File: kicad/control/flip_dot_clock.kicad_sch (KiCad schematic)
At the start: 36 parts, among them J1 Conn_01x02_Male, J2 Conn_02x08_Odd_Even, J3 Conn_01x05_Male, U1 NUCLEO-F303K8-HEADER, U10 Small_7_Seg_FlipDot_Module, U2 SLC03B-05, U3 NCV7719, U4 Small_7_Seg_FlipDot_Module, U5 NCV7719, U6 Small_7_Seg_FlipDot_Module, U7 NCV7719, U8 Small_7_Seg_FlipDot_Module, U9 NCV7719

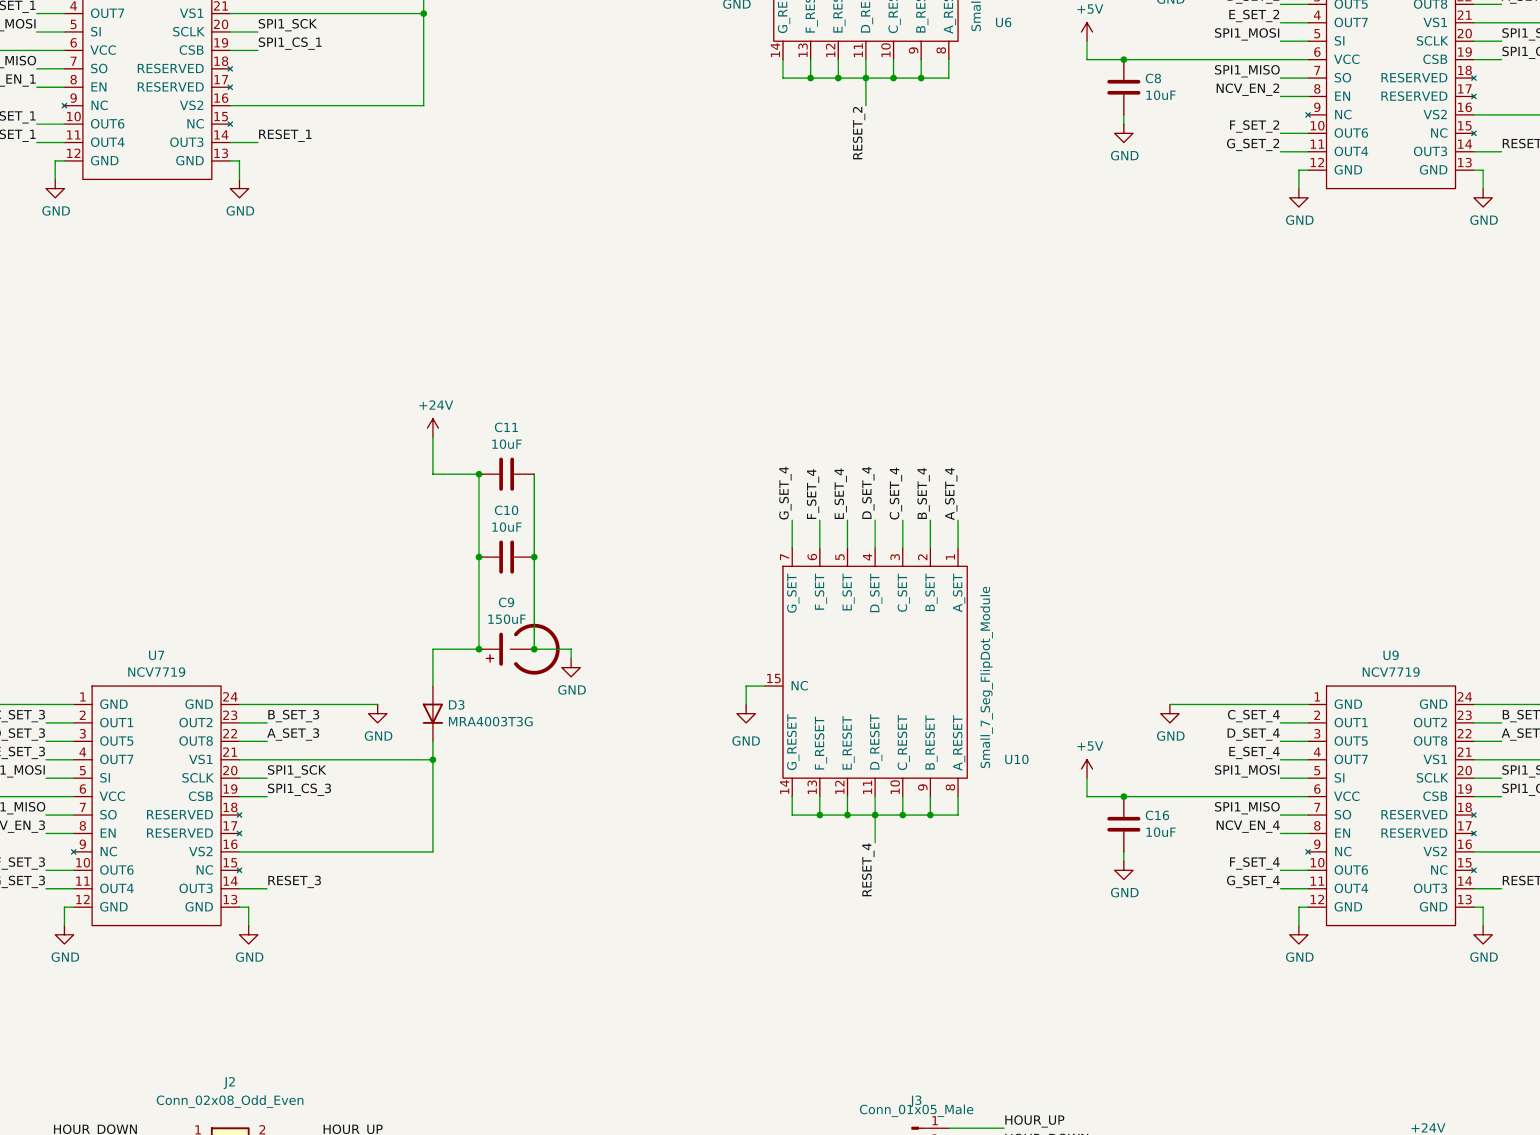
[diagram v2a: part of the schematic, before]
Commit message: add button board. update control ground plane.
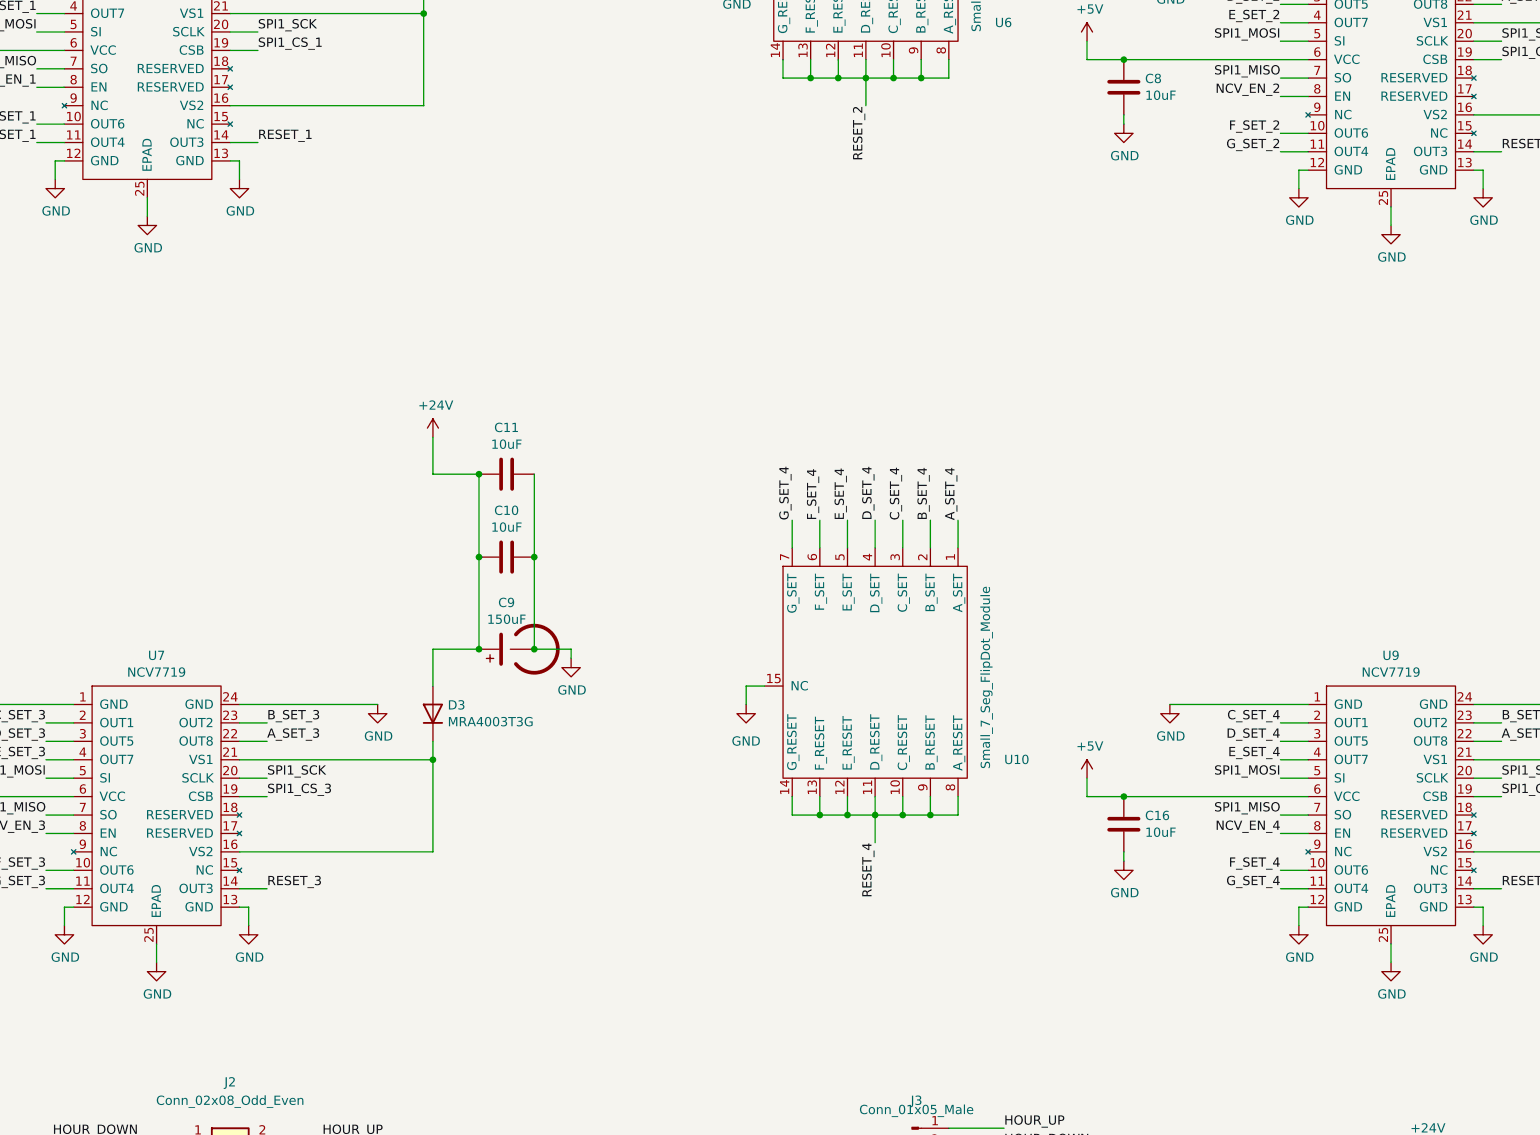
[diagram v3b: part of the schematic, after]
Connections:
- net GND: now also U3.25 (EPAD), U5.25 (EPAD), U7.25 (EPAD), U9.25 (EPAD)
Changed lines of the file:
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@@
+    (stroke (width 0) (type default))
+  )
+  (wire (pts (xy 344.17 199.39) (xy 344.17 201.93))
     (stroke (width 0) (type default))
   )
@@
     (stroke (width 0) (type default))
   )
+  (wire (pts (xy 172.72 96.52) (xy 172.72 99.06))
+    (stroke (width 0) (type default))
+  )
   (wire (pts (xy 113.03 77.47) (xy 113.03 74.93))
     (stroke (width 0) (type default))
@@
     (stroke (width 0) (type default))
   )
+  (wire (pts (xy 344.17 97.79) (xy 344.17 100.33))
+    (stroke (width 0) (type default))
+  )
   (wire (pts (xy 157.48 86.36) (xy 161.29 86.36))
     (stroke (width 0) (type default))
@@
   )
   (wire (pts (xy 104.14 181.61) (xy 104.14 185.42))
+    (stroke (width 0) (type default))
+  )
+  (wire (pts (xy 173.99 199.39) (xy 173.99 201.93))
     (stroke (width 0) (type default))
   )
@@
     (pin "1")
   )
-  (symbol (lib_name "Small_7_Seg_FlipDot_Module_2") (lib_id "mio:Small_7_Seg_FlipDot_Module") (at 271.78 43.18 0) (unit 1)
+  (symbol (lib_id "mio:Small_7_Seg_FlipDot_Module") (at 271.78 43.18 0) (unit 1)
     (in_bom yes) (on_board yes)
     (property "Reference" "U6" (id 0) (at 289.56 72.39 0)
@@
     (pin "9")
   )
-  (symbol (lib_name "Small_7_Seg_FlipDot_Module_1") (lib_id "mio:Small_7_Seg_FlipDot_Module") (at 273.05 144.78 0) (unit 1)
+  (symbol (lib_id "mio:Small_7_Seg_FlipDot_Module") (at 273.05 144.78 0) (unit 1)
     (in_bom yes) (on_board yes)
     (property "Reference" "U10" (id 0) (at 290.83 173.99 0)
@@
     (pin "1")
   )
-  (symbol (lib_name "Small_7_Seg_FlipDot_Module_3") (lib_id "mio:Small_7_Seg_FlipDot_Module") (at 104.14 144.78 0) (unit 1)
+  (symbol (lib_id "mio:Small_7_Seg_FlipDot_Module") (at 104.14 144.78 0) (unit 1)
     (in_bom yes) (on_board yes)
     (property "Reference" "U8" (id 0) (at 121.92 173.99 0)
@@
     (pin "23")
     (pin "24")
+    (pin "25")
     (pin "3")
     (pin "4")
@@
     )
     (property "Datasheet" "" (id 3) (at 135.89 85.09 0)
+      (effects (font (size 1.27 1.27)) hide)
+    )
+    (pin "1")
+  )
+  (symbol (lib_id "power:GND") (at 344.17 201.93 0) (unit 1)
+    (in_bom yes) (on_board yes)
+    (property "Reference" "#PWR?" (id 0) (at 344.17 208.28 0)
+      (effects (font (size 1.27 1.27)) hide)
+    )
+    (property "Value" "GND" (id 1) (at 344.297 206.3242 0)
+      (effects (font (size 1.27 1.27)))
+    )
+    (property "Footprint" "" (id 2) (at 344.17 201.93 0)
+      (effects (font (size 1.27 1.27)) hide)
+    )
+    (property "Datasheet" "" (id 3) (at 344.17 201.93 0)
       (effects (font (size 1.27 1.27)) hide)
     )
@@
     (pin "1")
   )
-  (symbol (lib_id "mio:NCV7719") (at 344.17 78.74 0) (unit 1)
+  (symbol (lib_name "NCV7719_1") (lib_id "mio:NCV7719") (at 344.17 78.74 0) (unit 1)
     (in_bom yes) (on_board yes)
     (property "Reference" "U5" (id 0) (at 344.17 58.039 0)
@@
     (pin "23")
     (pin "24")
+    (pin "25")
     (pin "3")
     (pin "4")
@@
     (pin "1")
   )
+  (symbol (lib_id "power:GND") (at 172.72 99.06 0) (unit 1)
+    (in_bom yes) (on_board yes)
+    (property "Reference" "#PWR?" (id 0) (at 172.72 105.41 0)
+      (effects (font (size 1.27 1.27)) hide)
+    )
+    (property "Value" "GND" (id 1) (at 172.847 103.4542 0)
+      (effects (font (size 1.27 1.27)))
+    )
+    (property "Footprint" "" (id 2) (at 172.72 99.06 0)
+      (effects (font (size 1.27 1.27)) hide)
+    )
+    (property "Datasheet" "" (id 3) (at 172.72 99.06 0)
+      (effects (font (size 1.27 1.27)) hide)
+    )
+    (pin "1")
+  )
   (symbol (lib_id "power:GND") (at 307.34 86.36 0) (unit 1)
     (in_bom yes) (on_board yes)
@@
   (symbol (lib_id "power:GND") (at 83.82 62.23 0) (unit 1)
     (in_bom yes) (on_board yes) (fields_autoplaced)
-    (property "Reference" "#PWR?" (id 0) (at 83.82 68.58 0)
+    (property "Reference" "#PWR0138" (id 0) (at 83.82 68.58 0)
       (effects (font (size 1.27 1.27)) hide)
     )
@@
     (pin "1")
   )
-  (symbol (lib_id "mio:NCV7719") (at 344.17 180.34 0) (unit 1)
+  (symbol (lib_name "NCV7719_2") (lib_id "mio:NCV7719") (at 344.17 180.34 0) (unit 1)
     (in_bom yes) (on_board yes)
     (property "Reference" "U9" (id 0) (at 344.17 159.639 0)
@@
     (pin "23")
     (pin "24")
+    (pin "25")
     (pin "3")
     (pin "4")
@@
     (pin "1")
   )
-  (symbol (lib_id "mio:NCV7719") (at 173.99 180.34 0) (unit 1)
+  (symbol (lib_name "NCV7719_3") (lib_id "mio:NCV7719") (at 173.99 180.34 0) (unit 1)
     (in_bom yes) (on_board yes)
     (property "Reference" "U7" (id 0) (at 173.99 159.639 0)
@@
     (pin "23")
     (pin "24")
+    (pin "25")
     (pin "3")
     (pin "4")
@@
     (pin "2")
   )
+  (symbol (lib_id "power:GND") (at 344.17 100.33 0) (unit 1)
+    (in_bom yes) (on_board yes)
+    (property "Reference" "#PWR?" (id 0) (at 344.17 106.68 0)
+      (effects (font (size 1.27 1.27)) hide)
+    )
+    (property "Value" "GND" (id 1) (at 344.297 104.7242 0)
+      (effects (font (size 1.27 1.27)))
+    )
+    (property "Footprint" "" (id 2) (at 344.17 100.33 0)
+      (effects (font (size 1.27 1.27)) hide)
+    )
+    (property "Datasheet" "" (id 3) (at 344.17 100.33 0)
+      (effects (font (size 1.27 1.27)) hide)
+    )
+    (pin "1")
+  )
   (symbol (lib_id "power:GND") (at 254 64.77 0) (unit 1)
     (in_bom yes) (on_board yes) (fields_autoplaced)
-    (property "Reference" "#PWR?" (id 0) (at 254 71.12 0)
+    (property "Reference" "#PWR0137" (id 0) (at 254 71.12 0)
       (effects (font (size 1.27 1.27)) hide)
     )
@@
   (symbol (lib_id "power:GND") (at 86.36 166.37 0) (unit 1)
     (in_bom yes) (on_board yes) (fields_autoplaced)
-    (property "Reference" "#PWR?" (id 0) (at 86.36 172.72 0)
+    (property "Reference" "#PWR0135" (id 0) (at 86.36 172.72 0)
       (effects (font (size 1.27 1.27)) hide)
     )
@@
     (pin "1")
   )
+  (symbol (lib_id "power:GND") (at 173.99 201.93 0) (unit 1)
+    (in_bom yes) (on_board yes)
+    (property "Reference" "#PWR?" (id 0) (at 173.99 208.28 0)
+      (effects (font (size 1.27 1.27)) hide)
+    )
+    (property "Value" "GND" (id 1) (at 174.117 206.3242 0)
+      (effects (font (size 1.27 1.27)))
+    )
+    (property "Footprint" "" (id 2) (at 173.99 201.93 0)
+      (effects (font (size 1.27 1.27)) hide)
+    )
+    (property "Datasheet" "" (id 3) (at 173.99 201.93 0)
+      (effects (font (size 1.27 1.27)) hide)
+    )
+    (pin "1")
+  )
   (symbol (lib_id "Device:C") (at 222.25 134.62 270) (unit 1)
     (in_bom yes) (on_board yes)
@@
   (symbol (lib_id "power:GND") (at 255.27 166.37 0) (unit 1)
     (in_bom yes) (on_board yes) (fields_autoplaced)
-    (property "Reference" "#PWR?" (id 0) (at 255.27 172.72 0)
+    (property "Reference" "#PWR0136" (id 0) (at 255.27 172.72 0)
       (effects (font (size 1.27 1.27)) hide)
     )
@@
       (reference "#PWR0134") (unit 1) (value "GND") (footprint "")
     )
+    (path "/9faa18e3-d506-4f2f-9547-fdb3f28a5c69"
+      (reference "#PWR0135") (unit 1) (value "GND") (footprint "")
+    )
+    (path "/e5767851-16b2-4e9c-863a-a06c33998d8d"
+      (reference "#PWR0136") (unit 1) (value "GND") (footprint "")
+    )
+    (path "/8e050dd7-51c3-4022-99d1-263f3d2804f7"
+      (reference "#PWR0137") (unit 1) (value "GND") (footprint "")
+    )
     (path "/795741d0-85b8-4f07-9fad-64977b7593b3"
+      (reference "#PWR0138") (unit 1) (value "GND") (footprint "")
+    )
+    (path "/0b23e1bb-408d-464c-8c81-13e2b5d23e23"
       (reference "#PWR?") (unit 1) (value "GND") (footprint "")
     )
-    (path "/8e050dd7-51c3-4022-99d1-263f3d2804f7"
+    (path "/5ec3df19-7cf3-459a-8399-72a32e477a5b"
       (reference "#PWR?") (unit 1) (value "GND") (footprint "")
     )
-    (path "/9faa18e3-d506-4f2f-9547-fdb3f28a5c69"
+    (path "/8d44a10e-b0c1-4575-a5d4-f2bd81a28341"
       (reference "#PWR?") (unit 1) (value "GND") (footprint "")
     )
-    (path "/e5767851-16b2-4e9c-863a-a06c33998d8d"
+    (path "/cd8db88a-a85b-4097-8ce4-a731999d11db"
       (reference "#PWR?") (unit 1) (value "GND") (footprint "")
     )
